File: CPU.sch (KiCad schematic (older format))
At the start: 13 parts, among them P8 SWD, U1 STM32F40X_LQFP64, Y1 8MHz

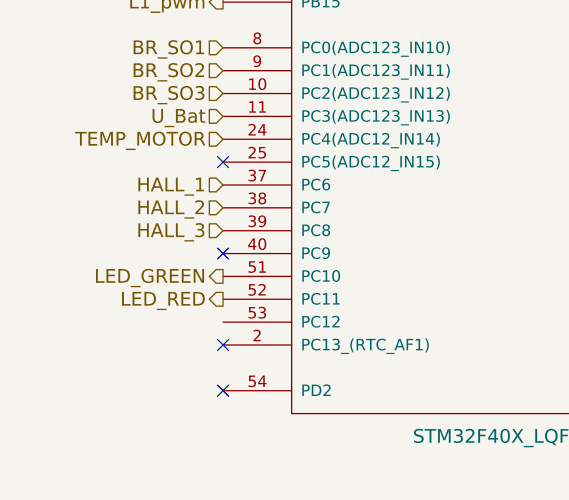
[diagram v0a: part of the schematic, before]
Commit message: continued Resolver continued Routing
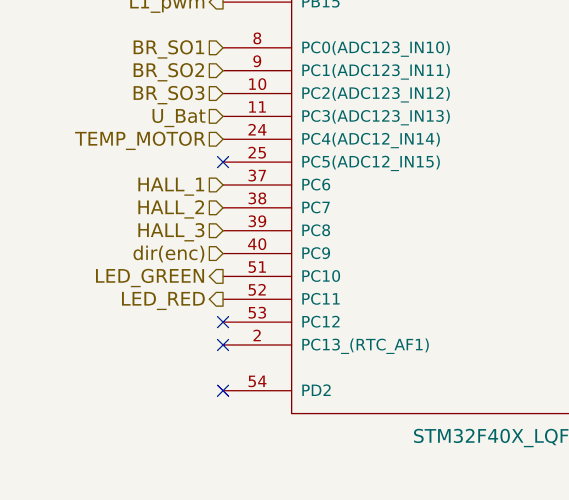
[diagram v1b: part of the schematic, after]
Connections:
- net dir(enc): now reaches U1.40 (PC9)
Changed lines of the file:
@@
 NoConn ~ 4500 6050
 NoConn ~ 4500 5850
-NoConn ~ 4500 5050
-NoConn ~ 4500 5450
 $Comp
 L Amalga_100-rescue:GND-RESCUE-BLDC_4-HSWR-V2-rescue #PWR043
@@
 Text HLabel 4500 3550 0    50   Input ~ 0
 RD_(R2D)
+Text HLabel 4500 5450 0    60   Input ~ 0
+dir(enc)
+NoConn ~ 4500 5750
+NoConn ~ 4500 5050
 $EndSCHEMATC

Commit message: Nearly Finished Layout. R2D 12V.
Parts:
- added C42: 1u, Capacitor_SMD:C_0805_2012Metric, symbol Amalga_100-rescue:C-RESCUE-BLDC_4-HSWR-V2-rescue
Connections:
- net +3V3: now also C42.2
- net GND: now also C42.1
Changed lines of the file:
@@
 NoConn ~ 4500 5750
 NoConn ~ 4500 5050
+$Comp
+L Amalga_100-rescue:C-RESCUE-BLDC_4-HSWR-V2-rescue C42
+U 1 1 5CB156A0
+P 10400 1300
+F 0 "C42" H 10450 1400 50  0000 L CNN
+F 1 "1u" H 10450 1200 50  0000 L CNN
+F 2 "Capacitor_SMD:C_0805_2012Metric" H 10400 1300 60  0001 C CNN
+F 3 "" H 10400 1300 60  0001 C CNN
+	1    10400 1300
+	-1   0    0    1
+$EndComp
+Wire Wire Line
+	10400 1600 10400 1500
+Wire Wire Line
+	10400 1000 10400 1100
+Wire Wire Line
+	10150 1600 10400 1600
+Wire Wire Line
+	10150 1000 10400 1000
 $EndSCHEMATC

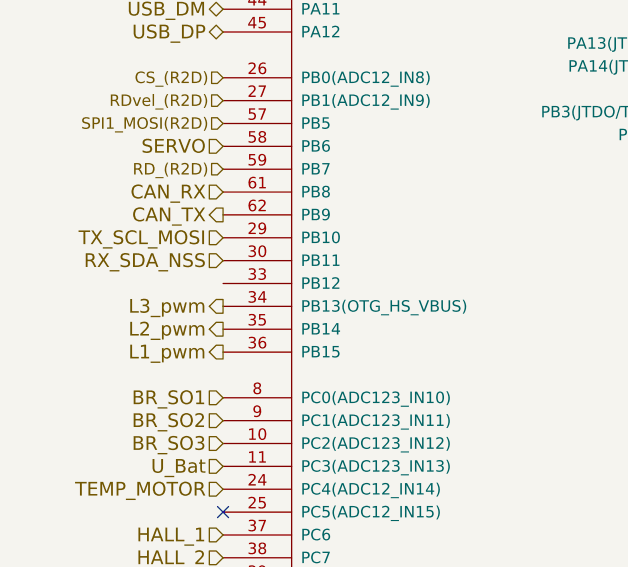
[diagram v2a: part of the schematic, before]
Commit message: -tidied up resolver circuit (need voltage detection on reset pin. >10µs, low active)
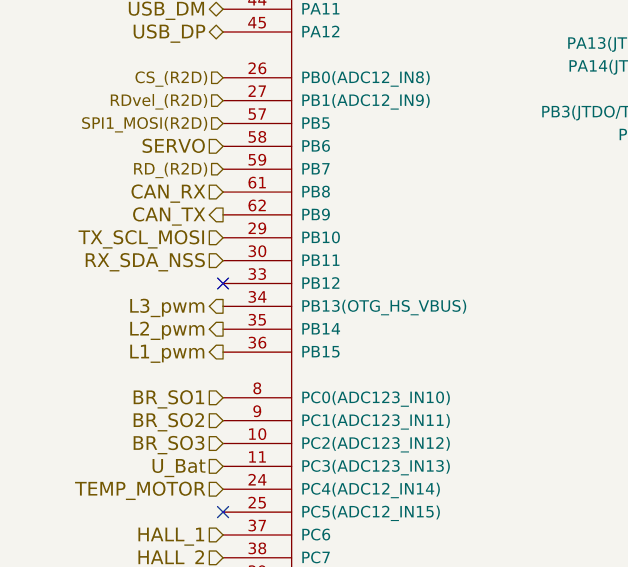
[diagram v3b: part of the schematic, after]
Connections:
- no-connect marks 8 -> 9
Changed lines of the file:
@@
 EESchema Schematic File Version 4
 LIBS:Amalga_100-cache
-EELAYER 26 0
+EELAYER 29 0
 EELAYER END
 $Descr A4 11693 8268
@@
 Wire Wire Line
 	10150 1000 10400 1000
+NoConn ~ 4500 4050
 $EndSCHEMATC

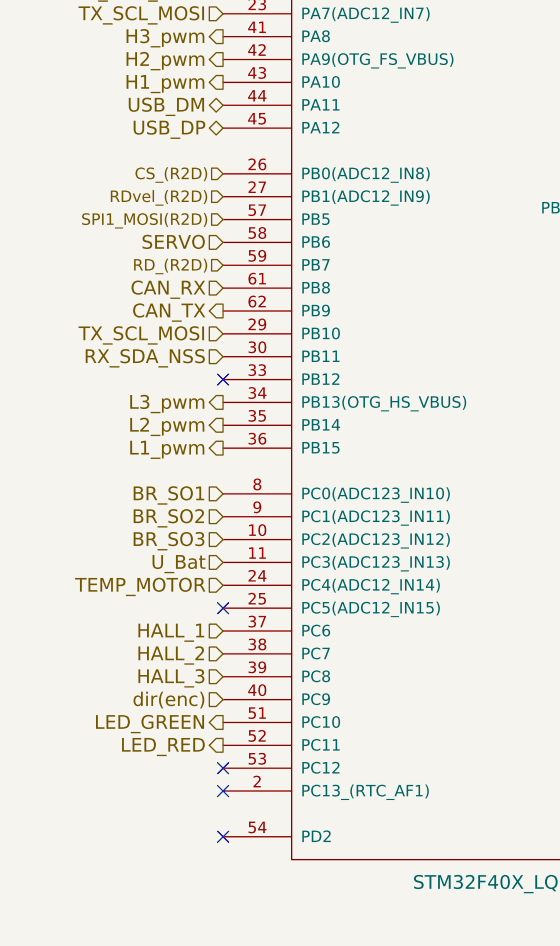
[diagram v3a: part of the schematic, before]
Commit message: -started implementing new sin/cos-Encoder Inputs -small changes like silkscreen
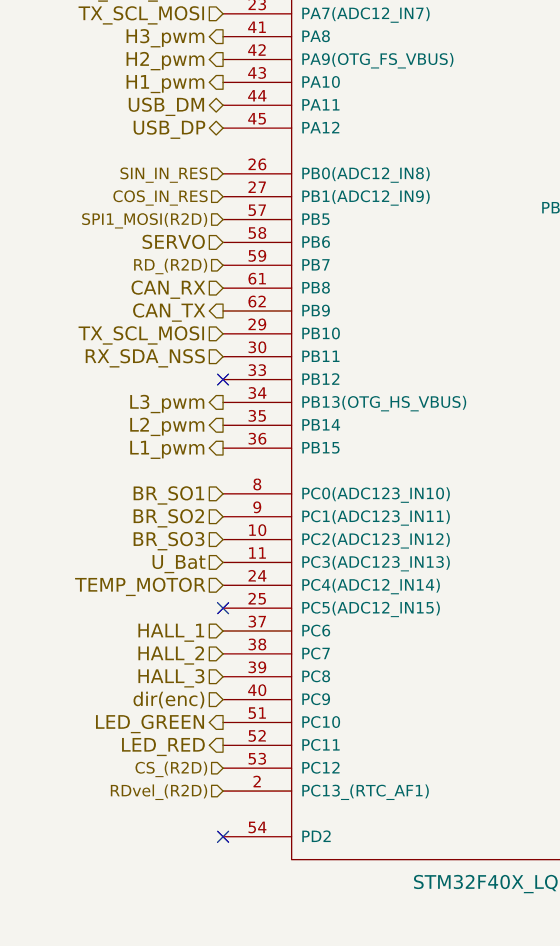
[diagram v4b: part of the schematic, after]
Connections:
- net CS_(R2D): now also U1.53 (PC12); no longer U1.26 (PB0(ADC12_IN8))
- net RDvel_(R2D): now also U1.2 (PC13_(RTC_AF1)); no longer U1.27 (PB1(ADC12_IN9))
- new net COS_IN_RES: U1.27 (PB1(ADC12_IN9))
- new net SIN_IN_RES: U1.26 (PB0(ADC12_IN8))
- no-connect marks 9 -> 7
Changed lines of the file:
@@
 EESchema Schematic File Version 4
 LIBS:Amalga_100-cache
-EELAYER 29 0
+EELAYER 26 0
 EELAYER END
 $Descr A4 11693 8268
@@
 NoConn ~ 7000 1850
 NoConn ~ 4500 6050
-NoConn ~ 4500 5850
 $Comp
 L Amalga_100-rescue:GND-RESCUE-BLDC_4-HSWR-V2-rescue #PWR043
@@
 Text HLabel 4500 4850 0    60   Input ~ 0
 U_Bat
-Text HLabel 4500 3150 0    50   Input ~ 0
+Text HLabel 4500 5750 0    50   Input ~ 0
 CS_(R2D)
-Text HLabel 4500 3250 0    50   Input ~ 0
+Text HLabel 4500 5850 0    50   Input ~ 0
 RDvel_(R2D)
 Text HLabel 4500 3550 0    50   Input ~ 0
@@
 Text HLabel 4500 5450 0    60   Input ~ 0
 dir(enc)
-NoConn ~ 4500 5750
 NoConn ~ 4500 5050
 $Comp
@@
 	10150 1000 10400 1000
 NoConn ~ 4500 4050
+Text HLabel 4500 3150 0    50   Input ~ 0
+SIN_IN_RES
+Text HLabel 4500 3250 0    50   Input ~ 0
+COS_IN_RES
 $EndSCHEMATC

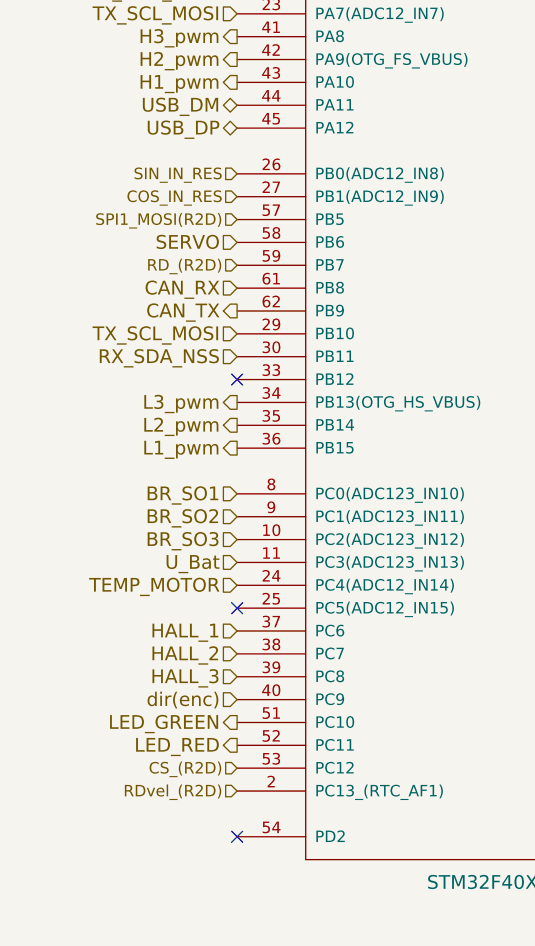
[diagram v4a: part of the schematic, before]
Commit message: added dc-bias for adc sin/cos resolver
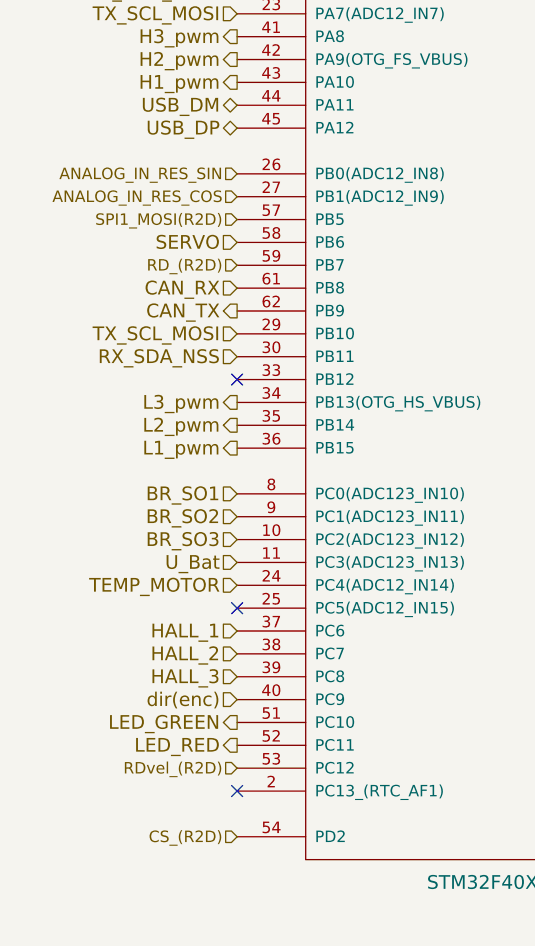
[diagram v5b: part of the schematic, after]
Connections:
- net CS_(R2D): now also U1.54 (PD2); no longer U1.53 (PC12)
- net RDvel_(R2D): now also U1.53 (PC12); no longer U1.2 (PC13_(RTC_AF1))
- net COS_IN_RES renamed ANALOG_IN_RES_COS
- net SIN_IN_RES renamed ANALOG_IN_RES_SIN
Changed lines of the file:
@@
 NoConn ~ 7000 1750
 NoConn ~ 7000 1850
-NoConn ~ 4500 6050
+NoConn ~ 4500 5850
 $Comp
 L Amalga_100-rescue:GND-RESCUE-BLDC_4-HSWR-V2-rescue #PWR043
@@
 Text HLabel 4500 4850 0    60   Input ~ 0
 U_Bat
-Text HLabel 4500 5750 0    50   Input ~ 0
+Text HLabel 4500 6050 0    50   Input ~ 0
 CS_(R2D)
-Text HLabel 4500 5850 0    50   Input ~ 0
+Text HLabel 4500 5750 0    50   Input ~ 0
 RDvel_(R2D)
 Text HLabel 4500 3550 0    50   Input ~ 0
@@
 NoConn ~ 4500 4050
 Text HLabel 4500 3150 0    50   Input ~ 0
-SIN_IN_RES
+ANALOG_IN_RES_SIN
 Text HLabel 4500 3250 0    50   Input ~ 0
-COS_IN_RES
+ANALOG_IN_RES_COS
 $EndSCHEMATC

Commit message: -changed wrong pin-header (swd)
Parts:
- P8: footprint Connector_PinSocket_2.54mm:PinSocket_2x03_P2.54mm_Vertical -> Connector_PinHeader_2.54mm:PinHeader_2x03_P2.54mm_Vertical
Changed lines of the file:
@@
 EESchema Schematic File Version 4
 LIBS:Amalga_100-cache
-EELAYER 29 0
+EELAYER 26 0
 EELAYER END
 $Descr A4 11693 8268
@@
 F 0 "P8" V 10050 3150 60  0000 C CNN
 F 1 "SWD" V 10150 3150 60  0000 C CNN
-F 2 "Connector_PinSocket_2.54mm:PinSocket_2x03_P2.54mm_Vertical" H 10100 3150 60  0001 C CNN
+F 2 "Connector_PinHeader_2.54mm:PinHeader_2x03_P2.54mm_Vertical" H 10100 3150 60  0001 C CNN
 F 3 "" H 10100 3150 60  0001 C CNN
 	1    10100 3150
